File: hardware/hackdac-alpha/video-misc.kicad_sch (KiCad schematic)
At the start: 43 parts, among them J13 TTL SYNC, J2 SYNC OUT, P1 BANK2_AUX, Q1 2N7002, Q2 BC857, Q3 BC857, U5 MCP47FEB22A1-E/ST, U6 74LVCH16T245, U7 74LVC1T45, X1 ECS-TXO-3225-270-TR

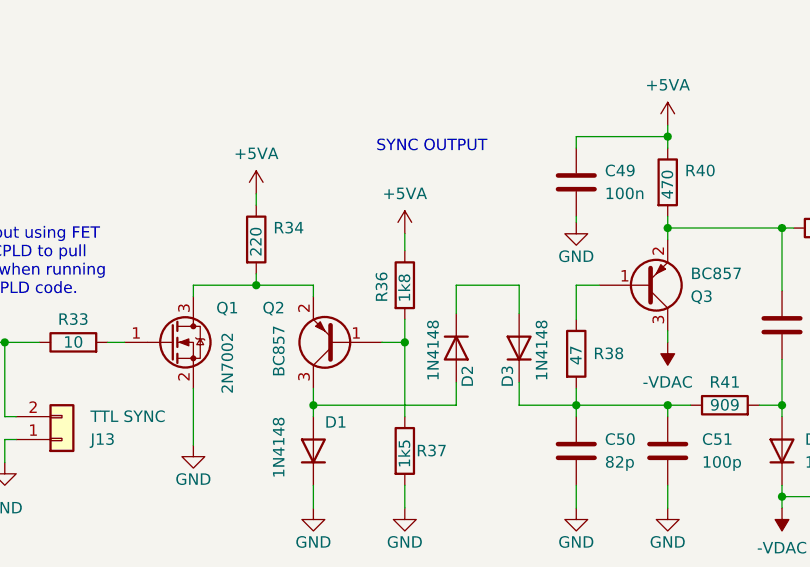
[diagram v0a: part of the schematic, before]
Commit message: Update component values
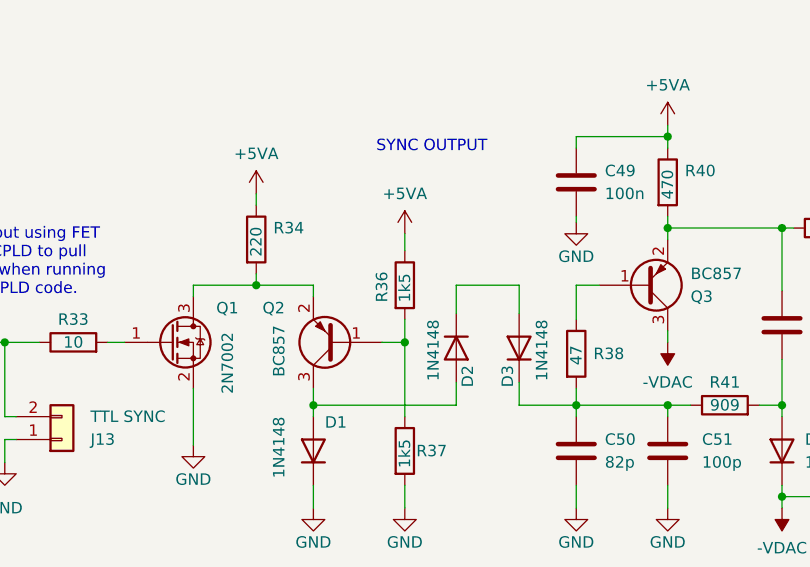
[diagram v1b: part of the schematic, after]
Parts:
- R36: value 1k8 -> 1k5
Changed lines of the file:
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@@
 			)
 		)
-		(property "Value" "1k8"
+		(property "Value" "1k5"
 			(at 208.915 101.6 90)
 			(effects

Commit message: Update with V2 mods
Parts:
- added C88: 0.1, symbol Device:C
- added Q7: 2N7002, Package_TO_SOT_SMD:SOT-23, symbol Transistor_FET:2N7002
- added U16: 74LVC1G125, Package_TO_SOT_SMD:SOT-23-5, symbol 74xGxx:74LVC1G125
- R31: value NF -> 10K
- R33: value 10 -> 2K2; footprint Resistor_SMD:R_0603_1608Metric -> (none)
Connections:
- net +3.3V_HACKRF: now also U16.5 (VCC)
- net +5VA: now also R33.1
- net GND: now also Q7.2 (S), U16.3 (GND)
- net LSYNC: now also Q7.1 (G); no longer R33.1
- net TCXO_CLK: now also C88.2; no longer R32.2
- net at Q1.1 (G), R33.2: now also Q7.3 (D)
- new net: C88.1, U16.4
- new net: R32.2, U16.2
- new net TCXO_ENABLE: U16.1
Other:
- note added: "NON TCXO OPTION: ECS-2333-270-BN-TR"
- note added: "NOT ON V2 PCB REWORK REQUIRED"
- note removed: "NOTE: 100R after output to allow TCXO safely clash with P56 (output) on standard HackRF CPLD code"
- note removed: "NOTE: Input using FET to allow CPLD to pull P55 high when running HackRF CPLD code."
- moved on the sheet: C48, C49, C50, C51, C52, C53, C54, D1, D2, D3, D4, J13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

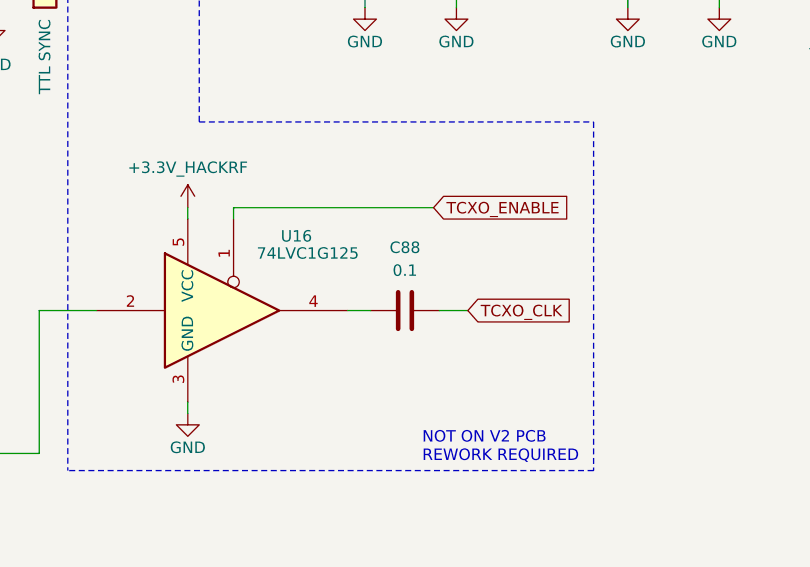
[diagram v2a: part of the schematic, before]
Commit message: Final values for V2 board
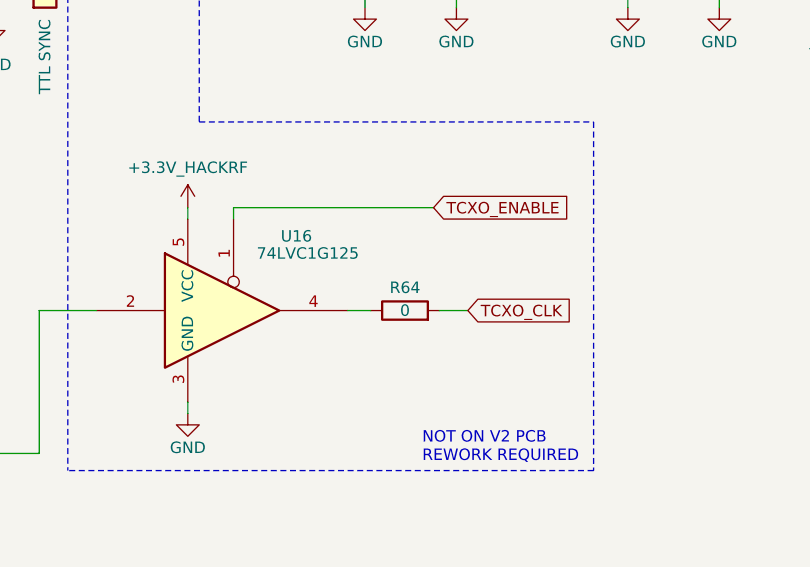
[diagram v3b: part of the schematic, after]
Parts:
- removed C88: 0.1, symbol Device:C
- added R64: 0, symbol Device:R
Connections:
- net TCXO_CLK: now also R64.2
- net at U16.4: now also R64.1
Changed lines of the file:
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@@
-	)
-	(symbol
-		(lib_id "Device:C")
-		(at 207.01 144.145 90)
-		(unit 1)
-		(exclude_from_sim no)
-		(in_bom yes)
-		(on_board yes)
-		(dnp no)
-		(fields_autoplaced yes)
-		(property "Reference" "C88"
-			(at 207.01 137.16 90)
-			(effects
-				(font
-					(size 1.27 1.27)
-				)
-			)
-		)
-		(property "Value" "0.1"
-			(at 207.01 139.7 90)
-			(effects
-				(font
-					(size 1.27 1.27)
-				)
-			)
-		)
-		(property "Footprint" ""
-			(at 210.82 143.1798 0)
-			(effects
-				(font
-					(size 1.27 1.27)
-				)
-				(hide yes)
-			)
-		)
-		(property "Datasheet" "~"
-			(at 207.01 144.145 0)
-			(effects
-				(font
-					(size 1.27 1.27)
-				)
-				(hide yes)
-			)
-		)
-		(property "Description" "Unpolarized capacitor"
-			(at 207.01 144.145 0)
-			(effects
-				(font
-					(size 1.27 1.27)
-				)
-				(hide yes)
-			)
-		)
-		(pin "1"
-		)
-		(pin "2"
-		)
-		(instances
-			(project ""
-				(path "/487245ca-0c1f-4f9d-bc99-20c8f558090f/e1e307fe-d49b-45b6-b177-774a7a482979"
-					(reference "C88")
-					(unit 1)
-				)
-			)
-		)
 	)
 	(symbol
@@
 					(unit 1)
 				)
+			)
+		)
+	)
+	(symbol
+		(lib_id "Device:R")
+		(at 207.01 144.145 90)
+		(unit 1)
+		(exclude_from_sim no)
+		(in_bom yes)
+		(on_board yes)
+		(dnp no)
+		(property "Reference" "R64"
+			(at 207.01 141.605 90)
+			(effects
+				(font
+					(size 1.27 1.27)
+				)
+			)
+		)
+		(property "Value" "0"
+			(at 207.01 144.145 90)
+			(effects
+				(font
+					(size 1.27 1.27)
+				)
+			)
+		)
+		(property "Footprint" ""
+			(at 207.01 145.923 90)
+			(effects
+				(font
+					(size 1.27 1.27)
+				)
+				(hide yes)
+			)
+		)
+		(property "Datasheet" "~"
+			(at 207.01 144.145 0)
+			(effects
+				(font
+					(size 1.27 1.27)
+				)
+				(hide yes)
+			)
+		)
+		(property "Description" "Resistor"
+			(at 207.01 144.145 0)
+			(effects
+				(font
+					(size 1.27 1.27)
+				)
+				(hide yes)
+			)
+		)
+		(pin "2"
+		)
+		(pin "1"
+		)
+		(instances
+			(project ""
+				(path "/487245ca-0c1f-4f9d-bc99-20c8f558090f/e1e307fe-d49b-45b6-b177-774a7a482979"
+					(reference "R64")
+					(unit 1)
+				)

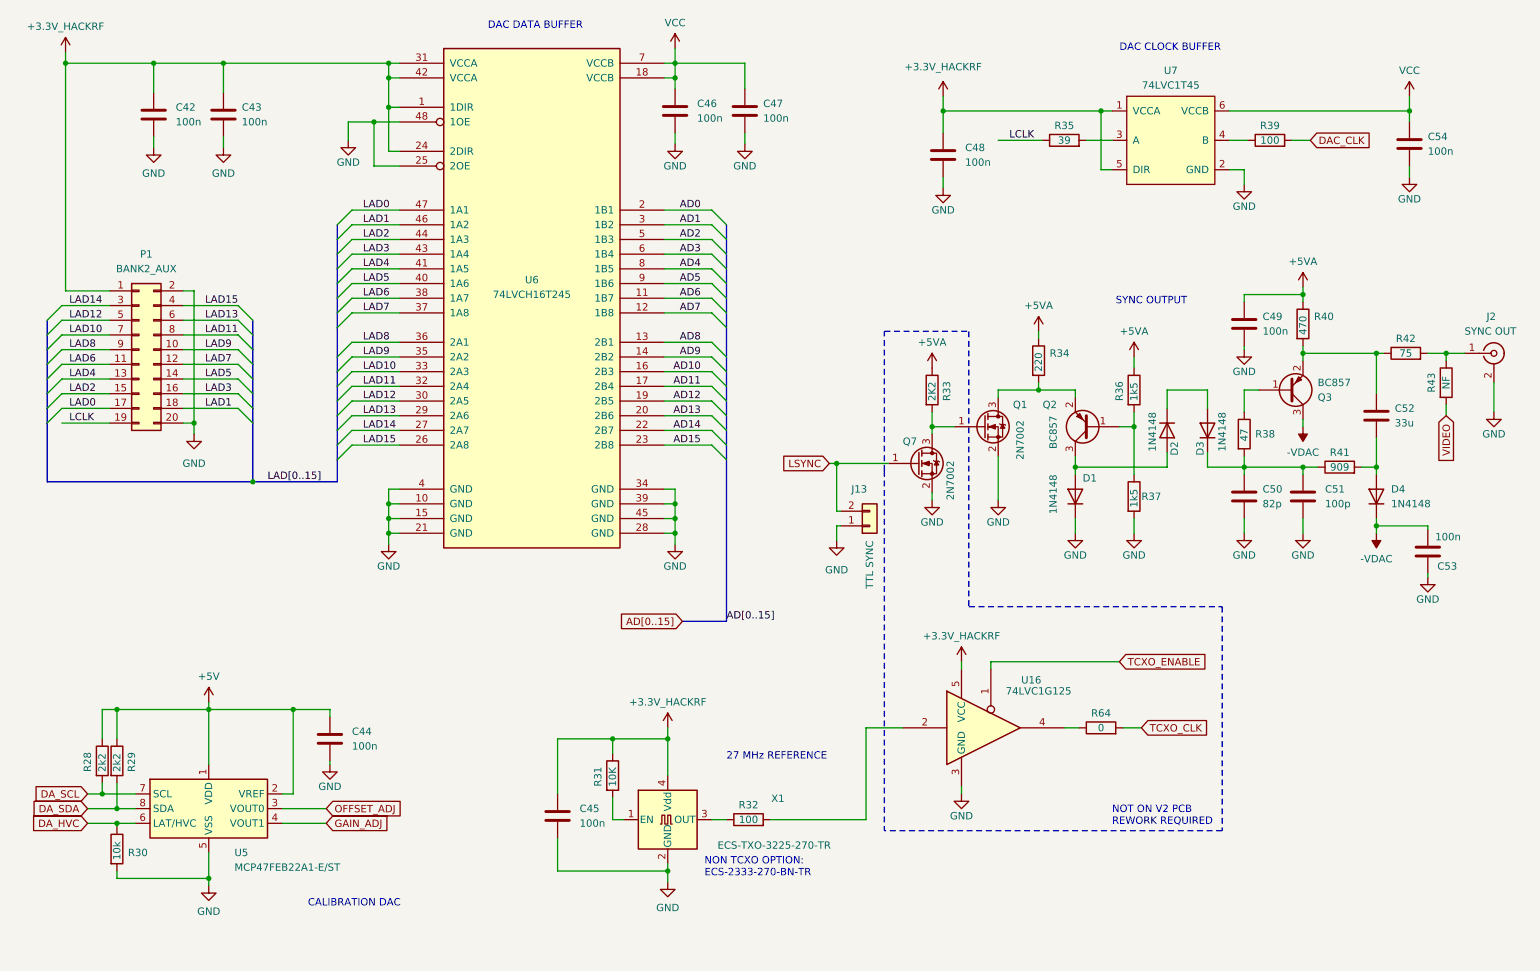
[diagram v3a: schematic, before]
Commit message: More V3 component rationalisation
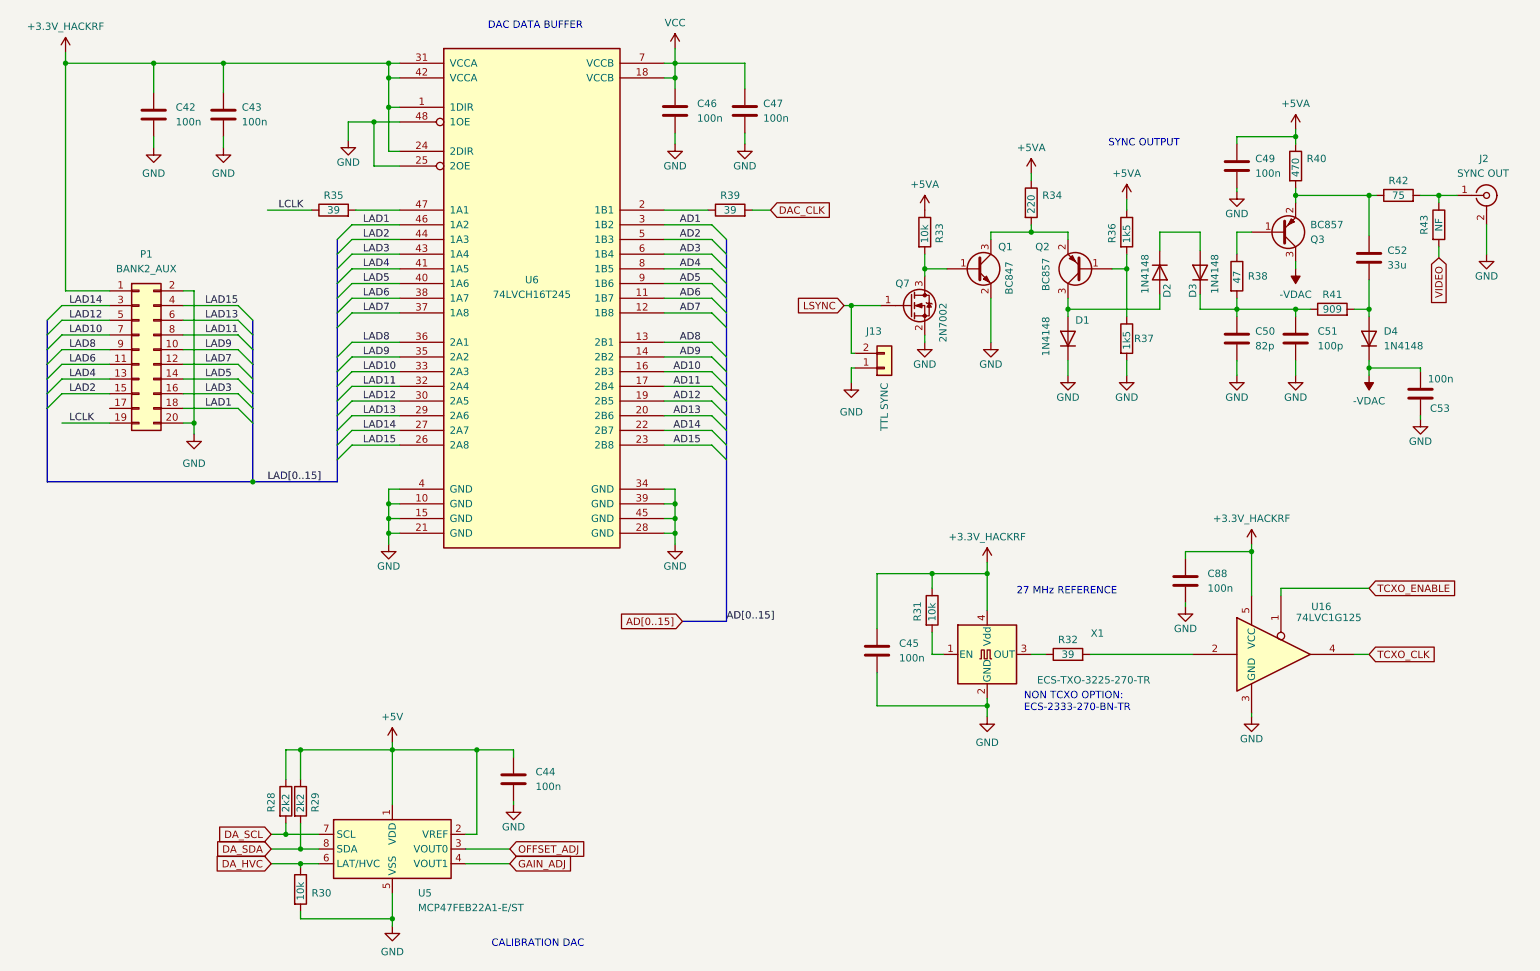
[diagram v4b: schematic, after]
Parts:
- removed C48, C54: 100n, Capacitor_SMD:C_0603_1608Metric, symbol Device:C
- removed Q1: 2N7002, Package_TO_SOT_SMD:SOT-23, symbol Transistor_FET:2N7002
- removed R64: 0, symbol Device:R
- removed U7: 74LVC1T45, Package_TO_SOT_SMD:SOT-23-6, symbol 74lvc1t45:74LVC1T45
- added C88: 100n, Capacitor_SMD:C_0603_1608Metric, symbol Device:C
- added Q1: BC847, Package_TO_SOT_SMD:SOT-23, symbol Transistor_BJT:BC847
- R31: value 10K -> 10k
- R32, R39: value 100 -> 39
- R33: value 2K2 -> 10k
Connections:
- net AD0 is gone; now on an unnamed net: U6.2 (1B1)
- net +3.3V_HACKRF: now also C88.1
- net GND: now also C88.2, Q1.2 (E)
- net TCXO_CLK: now also U16.4
- net at Q7.3 (D), R33.2: now also Q1.1 (B)
- net at Q2.2 (E), R34.2: now also Q1.3 (C)
- net at R35.2: now also U6.47 (1A1)
- net LAD0: no longer names the net of P1.17 (Pin_17)
- net LAD0: no longer U6.47 (1A1)
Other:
- note removed: "DAC CLOCK BUFFER"
- note removed: "NOT ON V2 PCB REWORK REQUIRED"
- moved on the sheet: C44, C45, C49, C50, C51, C52, C53, D1, D2, D3, D4, J13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

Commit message: Last of major V3 changes
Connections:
- net -VDAC: no longer C53.2, D4.1 (K)
- new net -5VA: C53.2, D4.1 (K)
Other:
- moved on the sheet: C42, C43, C44, C46, C47, C49, C50, C51, C52, C53, D1, D2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

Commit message: V3 PCB WIP
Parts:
- R33: footprint (none) -> Resistor_SMD:R_0603_1608Metric
- renumbered C46 to C45, C47 to C46, C45 to C47, C88 to C48, J13 to J2, J2 to J3, Q7 to Q1, Q1 to Q2, Q2 to Q3, Q3 to Q4, R35 to R31, R39 to R32, R31 to R34, R34 to R35, R32 to R36, R36 to R37, R37 to R38, R38 to R39, U16 to U7
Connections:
- net -VDAC is gone; now on net -5VA: Q4.3 (C)
- net VCC is gone; now on net +5V: C45.1, C46.1, U6.18 (VCCB), U6.7 (VCCB)

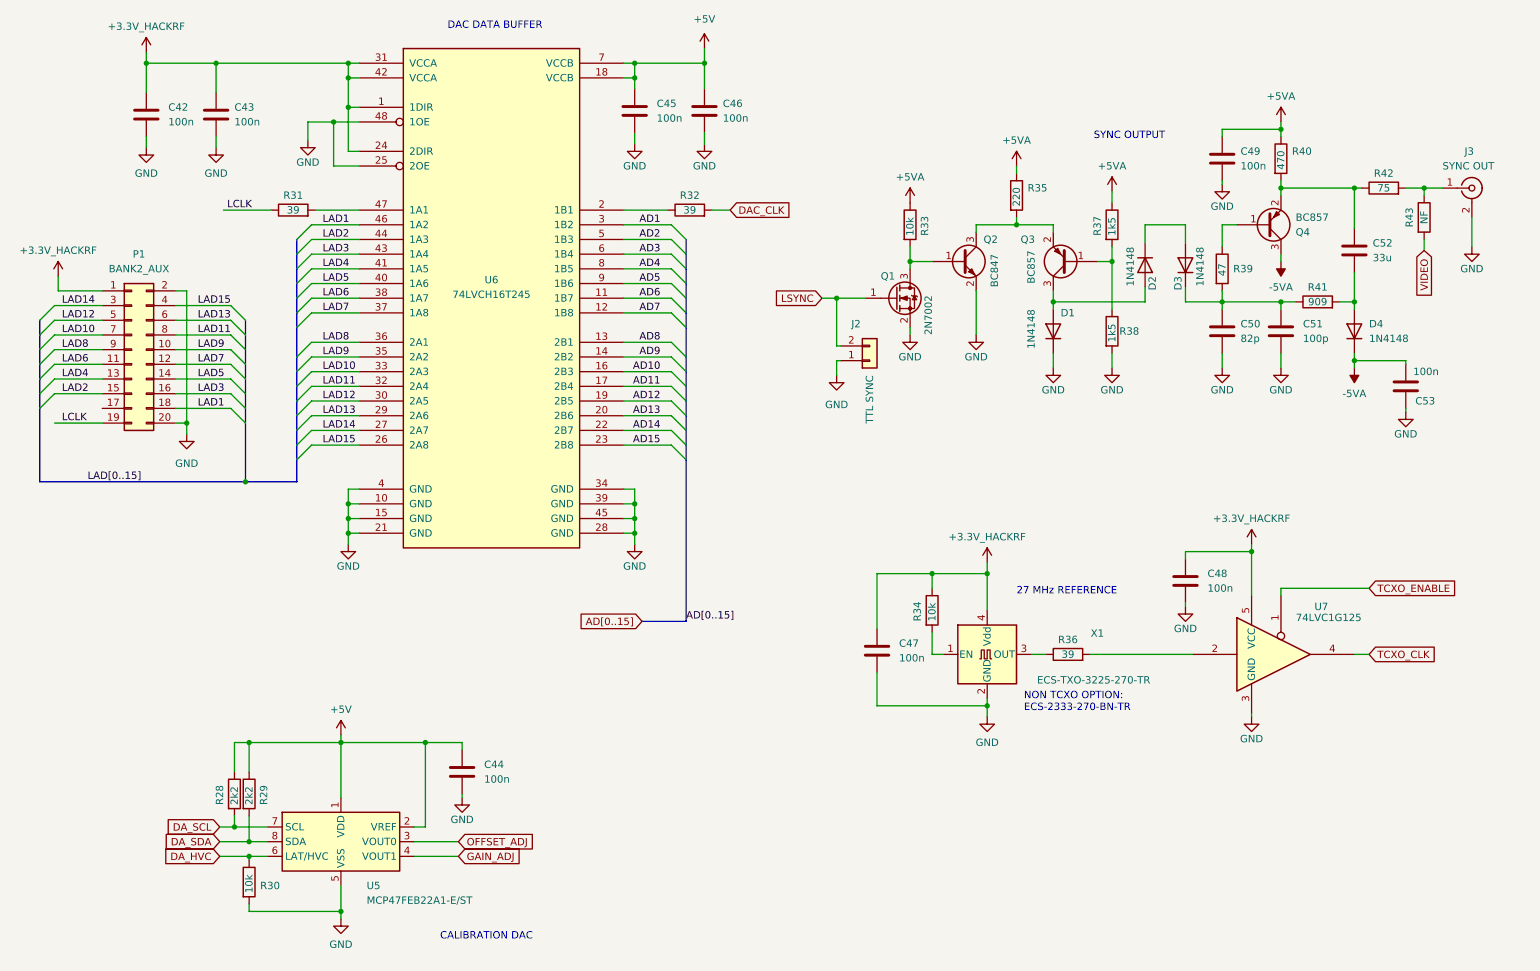
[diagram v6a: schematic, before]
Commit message: Optional caps for DAC supply
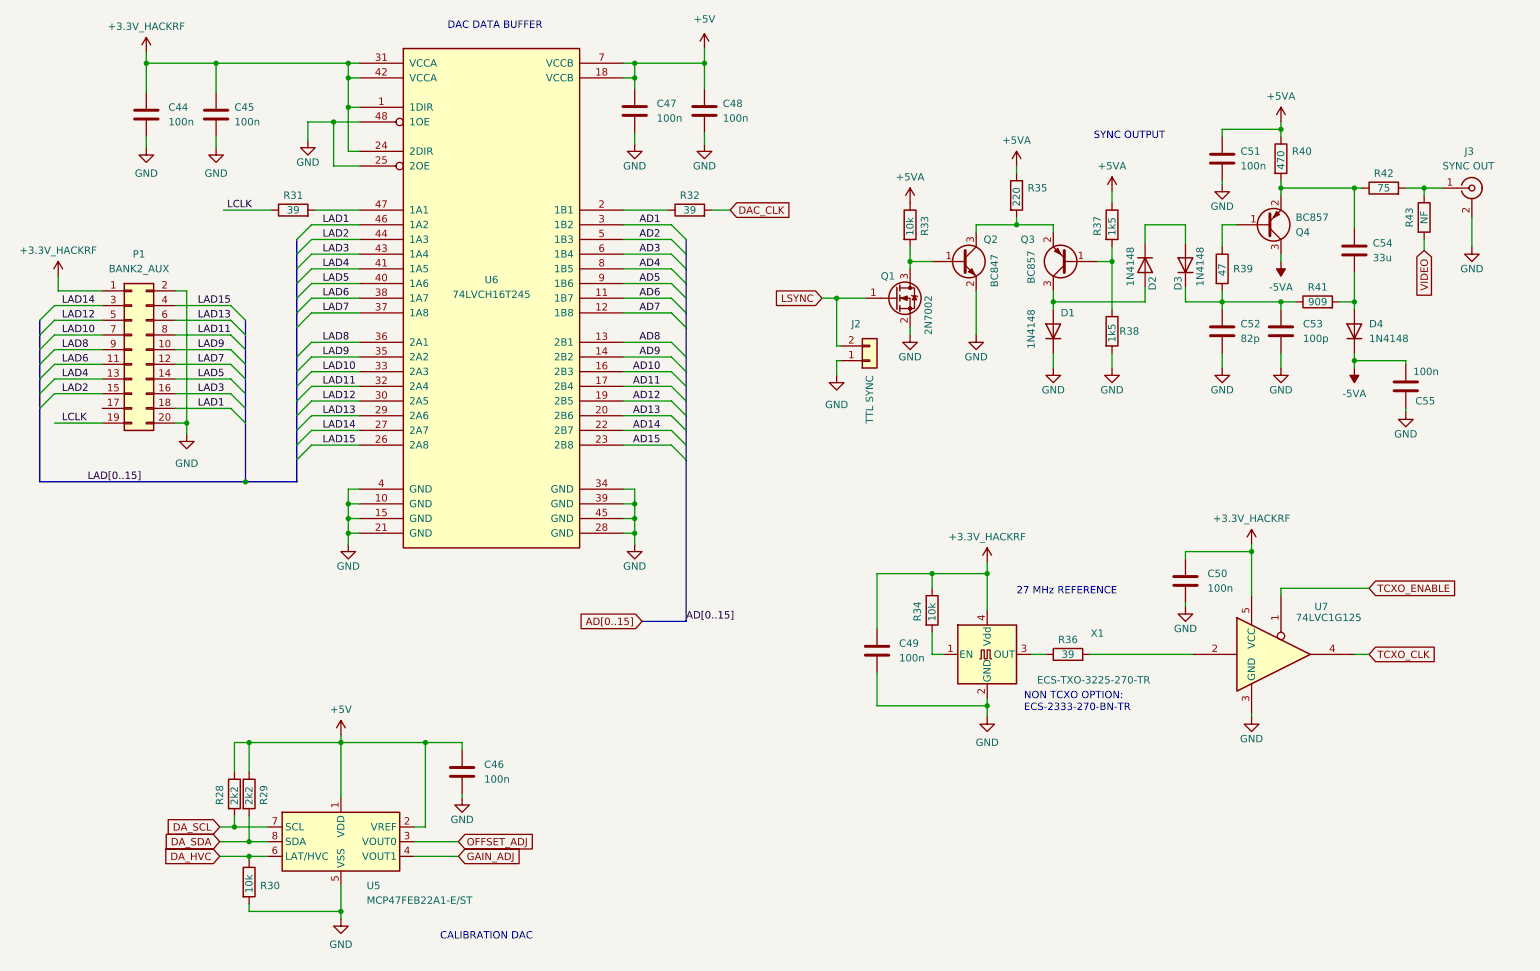
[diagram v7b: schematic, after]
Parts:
- renumbered C42 to C44, C43 to C45, C44 to C46, C45 to C47, C46 to C48, C47 to C49, C48 to C50, C49 to C51, C50 to C52, C51 to C53, C52 to C54, C53 to C55
